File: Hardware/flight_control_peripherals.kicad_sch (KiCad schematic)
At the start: 18 parts, among them J10 Conn_01x06, J2 DM3AT-SF-PEJM5, J5 Conn_01x10, J6 Conn_02x10_Odd_Even, J7 Conn_01x04, J8 Conn_01x04, J9 Conn_02x06_Odd_Even, U13 W25N01GVZEIG_TR, U14 24CW1280T-I/OT, U15 PCA9685PW_118

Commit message: hardware: reorganizing components, im fucked
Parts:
- C55, C56, C58, C59: footprint Capacitor_SMD:C_0603_1608Metric -> Capacitor_SMD:C_0402_1005Metric
- C57: footprint Capacitor_SMD:C_1206_3216Metric_Pad1.33x1.80mm_HandSolder -> Capacitor_SMD:C_0603_1608Metric
- R33, R34, R54: footprint Resistor_SMD:R_0603_1608Metric_Pad0.98x0.95mm_HandSolder -> Resistor_SMD:R_0402_1005Metric
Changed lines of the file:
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@@
 			)
 		)
-		(property "Footprint" "Capacitor_SMD:C_0603_1608Metric"
+		(property "Footprint" "Capacitor_SMD:C_0402_1005Metric"
 			(at 117.8052 116.84 0)
 			(effects
@@
 			)
 		)
-		(property "Footprint" "Resistor_SMD:R_0603_1608Metric_Pad0.98x0.95mm_HandSolder"
+		(property "Footprint" "Resistor_SMD:R_0402_1005Metric"
 			(at 104.902 111.76 90)
 			(effects
@@
 			)
 		)
-		(property "Footprint" "Capacitor_SMD:C_0603_1608Metric"
+		(property "Footprint" "Capacitor_SMD:C_0402_1005Metric"
 			(at 125.73 177.4952 0)
 			(effects
@@
 			)
 		)
-		(property "Footprint" "Resistor_SMD:R_0603_1608Metric_Pad0.98x0.95mm_HandSolder"
+		(property "Footprint" "Resistor_SMD:R_0402_1005Metric"
 			(at 96.012 111.76 90)
 			(effects
@@
 			)
 		)
-		(property "Footprint" "Capacitor_SMD:C_1206_3216Metric_Pad1.33x1.80mm_HandSolder"
+		(property "Footprint" "Capacitor_SMD:C_0603_1608Metric"
 			(at 239.7252 132.08 0)
 			(effects
@@
 			)
 		)
-		(property "Footprint" "Capacitor_SMD:C_0603_1608Metric"
+		(property "Footprint" "Capacitor_SMD:C_0402_1005Metric"
 			(at 205.74 30.1752 0)
 			(effects
@@
 			)
 		)
-		(property "Footprint" "Resistor_SMD:R_0603_1608Metric_Pad0.98x0.95mm_HandSolder"
+		(property "Footprint" "Resistor_SMD:R_0402_1005Metric"
 			(at 191.262 142.24 90)
 			(effects
@@
 			)
 		)
-		(property "Footprint" "Capacitor_SMD:C_0603_1608Metric"
+		(property "Footprint" "Capacitor_SMD:C_0402_1005Metric"
 			(at 249.8852 132.08 0)
 			(effects

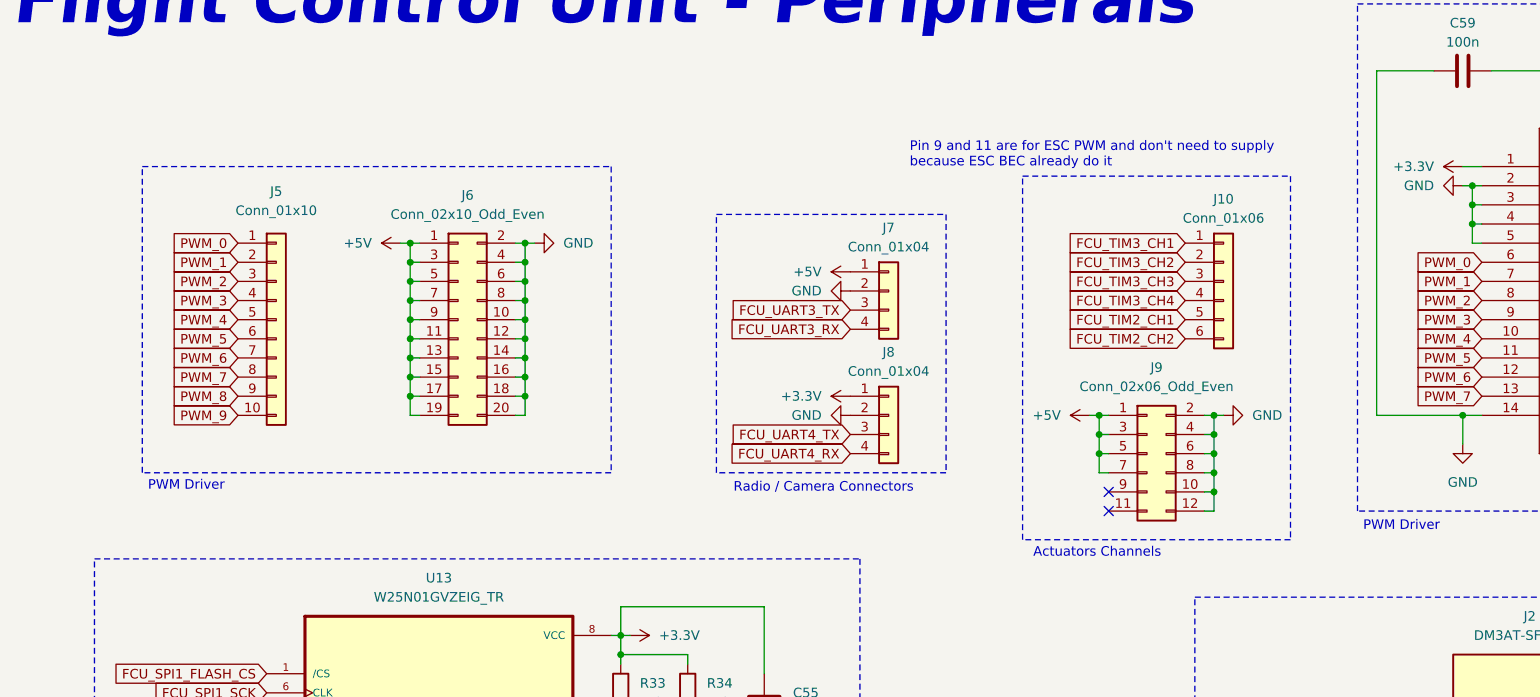
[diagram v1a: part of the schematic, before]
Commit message: hardware: initial power supply layout
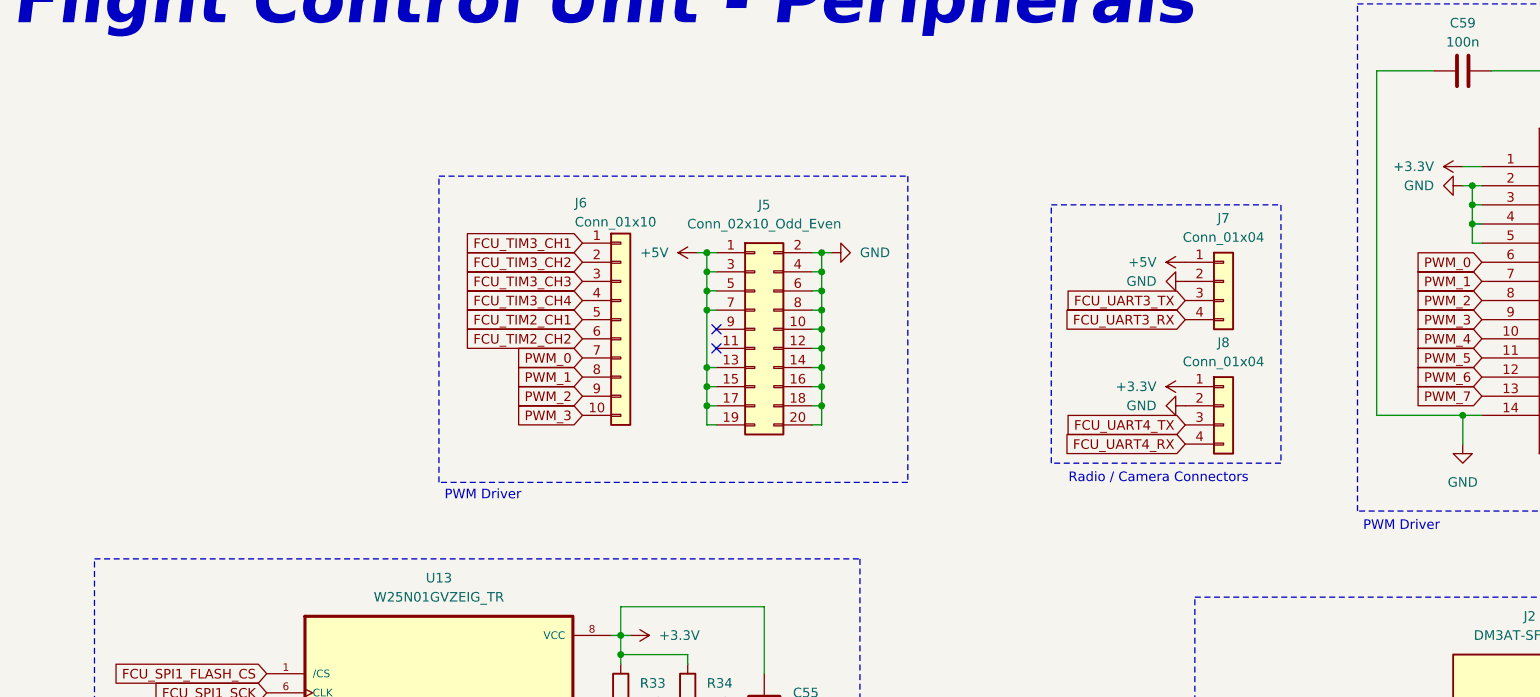
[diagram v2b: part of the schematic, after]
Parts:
- removed J10: Conn_01x06, Connector_PinHeader_2.54mm:PinHeader_1x06_P2.54mm_Vertical, symbol Connector_Generic:Conn_01x06
- removed J5: Conn_01x10, Connector_PinHeader_2.54mm:PinHeader_1x10_P2.54mm_Vertical, symbol Connector_Generic:Conn_01x10
- removed J6: Conn_02x10_Odd_Even, Connector_PinHeader_2.54mm:PinHeader_2x10_P2.54mm_Vertical, symbol Connector_Generic:Conn_02x10_Odd_Even
- removed J9: Conn_02x06_Odd_Even, Connector_PinHeader_2.54mm:PinHeader_2x06_P2.54mm_Vertical, symbol Connector_Generic:Conn_02x06_Odd_Even
- added J5: Conn_02x10_Odd_Even, Connector_PinHeader_2.54mm:PinHeader_2x10_P2.54mm_Vertical, symbol Connector_Generic:Conn_02x10_Odd_Even
- added J6: Conn_01x10, Connector_PinHeader_2.54mm:PinHeader_1x10_P2.54mm_Vertical, symbol Connector_Generic:Conn_01x10
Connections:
- net +5V: now also J5.1 (Pin_1), J5.13 (Pin_13), J5.15 (Pin_15), J5.17 (Pin_17), J5.19 (Pin_19), J5.3 (Pin_3), J5.5 (Pin_5), J5.7 (Pin_7)
- net FCU_TIM2_CH1: now also J6.5 (Pin_5)
- net FCU_TIM2_CH2: now also J6.6 (Pin_6)
- net FCU_TIM3_CH1: now also J6.1 (Pin_1)
- net FCU_TIM3_CH2: now also J6.2 (Pin_2)
- net FCU_TIM3_CH3: now also J6.3 (Pin_3)
- net FCU_TIM3_CH4: now also J6.4 (Pin_4)
- net GND: now also J5.10 (Pin_10), J5.12 (Pin_12), J5.14 (Pin_14), J5.16 (Pin_16), J5.18 (Pin_18), J5.2 (Pin_2), J5.20 (Pin_20), J5.4 (Pin_4), J5.6 (Pin_6), J5.8 (Pin_8)
- net PWM_0: now also J6.7 (Pin_7)
- net PWM_1: now also J6.8 (Pin_8)
- net PWM_2: now also J6.9 (Pin_9)
- net PWM_3: now also J6.10 (Pin_10)
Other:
- note removed: "Actuators Channels"
- note removed: "Pin 9 and 11 are for ESC PWM and don't need to supply because ESC BEC already do it"
- moved on the sheet: J7, J8
